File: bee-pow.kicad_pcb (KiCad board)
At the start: 2 copper layers, 29 x 53.3 mm, 12 parts, among them J1 Conn_01x02_Male, J2 Conn_01x02_Male, J3 Conn_01x02_Male, J4 Conn_01x02_Male

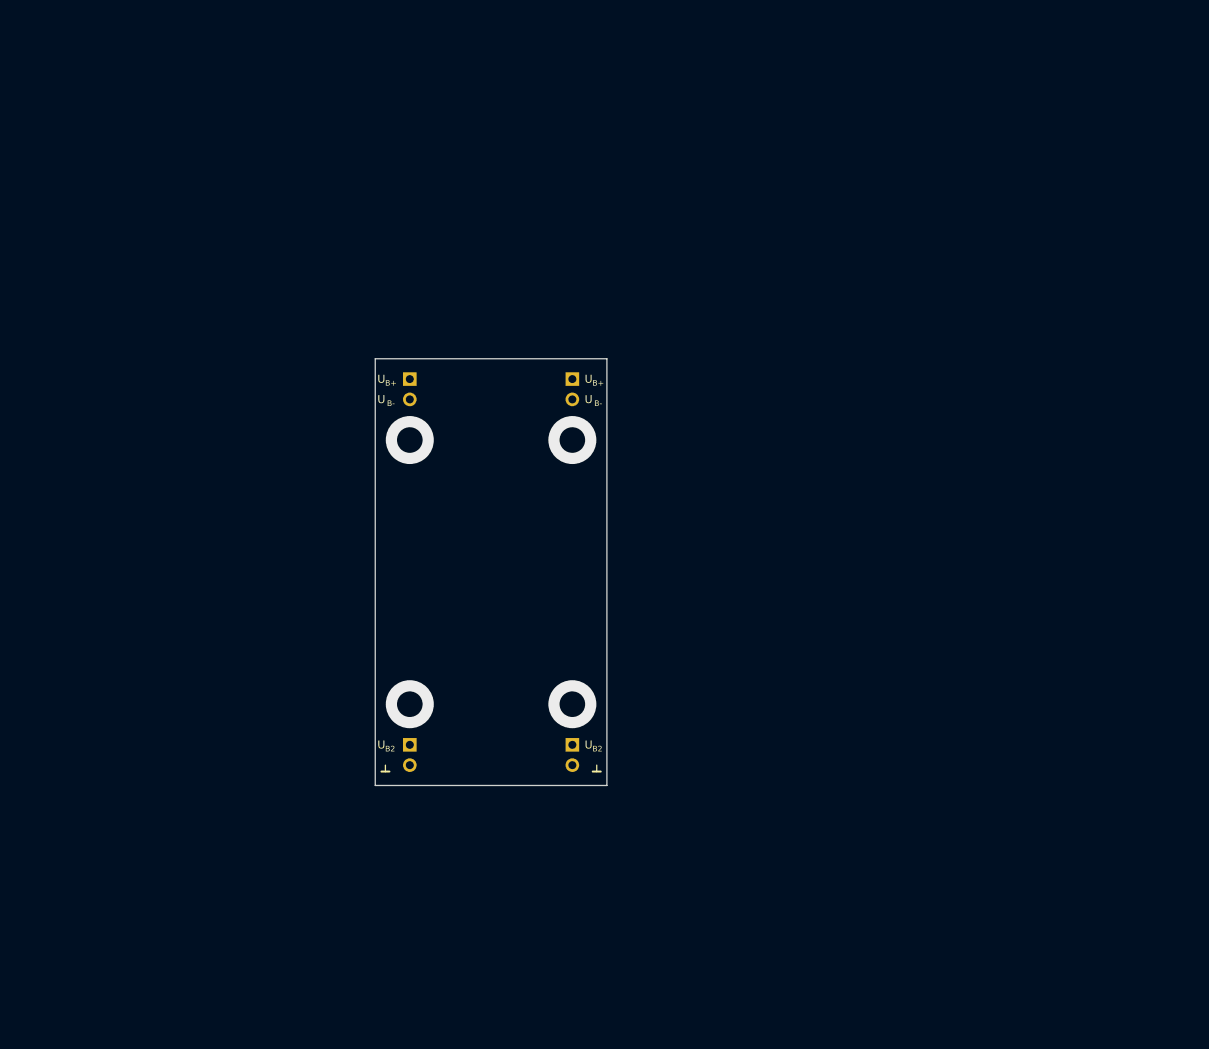
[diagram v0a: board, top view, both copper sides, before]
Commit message: begin schematic
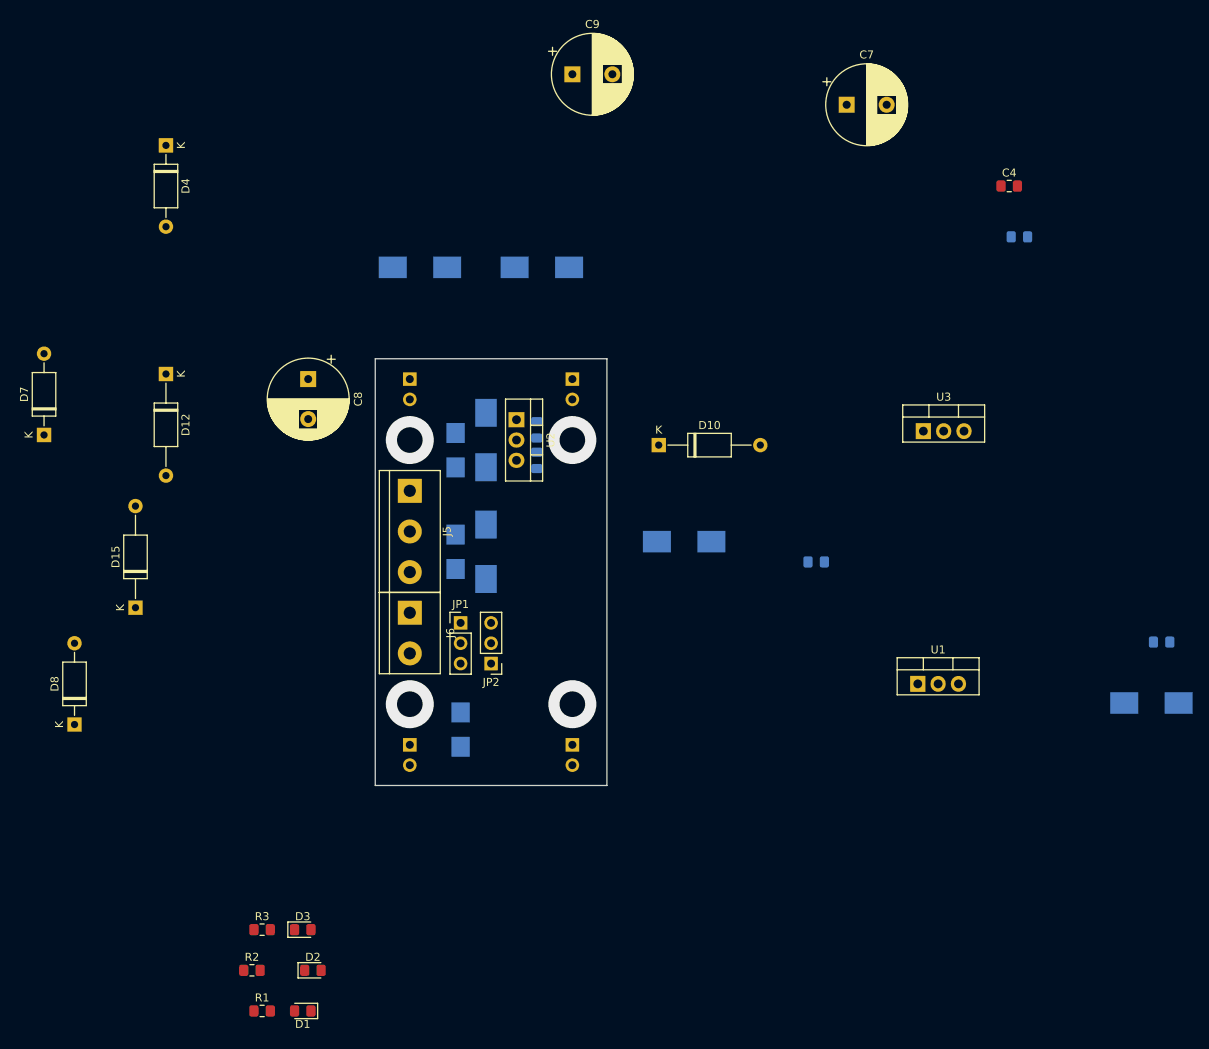
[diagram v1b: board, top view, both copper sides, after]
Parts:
- removed REF** (x2): Text_U_B+_Silkscreen, Symbol-emt:Text_U_B+_Silkscreen
- removed REF** (x2): Text_U_B-_Silkscreen, Symbol-emt:Text_U_B-_Silkscreen
- removed REF** (x2): Text_U_B2_Silkscreen, Symbol-emt:Text_U_B2_Silkscreen
- removed REF** (x2): Symbol_GND_Silkscreen, Symbol-emt:Symbol_GND_Silkscreen
- added C1: 0.33µF, Capacitor_SMD:C_0805_2012Metric_Pad1.15x1.40mm_HandSolder, B.Cu at (172.7, 124.3)
- added C2: 0.33µF, Capacitor_SMD:C_0805_2012Metric_Pad1.15x1.40mm_HandSolder, B.Cu at (94.6, 97.8)
- added C3: 0.33µF, Capacitor_SMD:C_0805_2012Metric_Pad1.15x1.40mm_HandSolder, B.Cu at (154.9, 73.7)
- added C4: 0.1µF, Capacitor_SMD:C_0805_2012Metric_Pad1.15x1.40mm_HandSolder, F.Cu at (153.7, 67.3)
- added C5: 0.1µF, Capacitor_SMD:C_0805_2012Metric_Pad1.15x1.40mm_HandSolder, B.Cu at (94.6, 101.6)
- added C6: 0.1µF, Capacitor_SMD:C_0805_2012Metric_Pad1.15x1.40mm_HandSolder, B.Cu at (129.5, 114.3)
- added C7: 220µF, Capacitor_THT:CP_Radial_D10.0mm_P5.00mm, F.Cu at (133.3, 57.1)
- added C8: 220µF, Capacitor_THT:CP_Radial_D10.0mm_P5.00mm, F.Cu at (66.0, 91.4)
- added C9: 220µF, Capacitor_THT:CP_Radial_D10.0mm_P5.00mm, F.Cu at (99.1, 53.3)
- added D1: LED, LED_SMD:LED_0805_2012Metric_Pad1.15x1.40mm_HandSolder, F.Cu at (65.4, 170.4)
- added D10: 1N4001, Diode_THT:D_A-405_P12.70mm_Horizontal, F.Cu at (109.9, 99.7)
- added D11: 1N4001, Diode_SMD:D_MELF_Handsoldering, B.Cu at (80.0, 77.5)
- added D12: 1N4001, Diode_THT:D_A-405_P12.70mm_Horizontal, F.Cu at (48.3, 90.8)
- added D13: 1N4001, Diode_SMD:D_MELF_Handsoldering, B.Cu at (88.3, 99.1)
- added D14: 1N4001, Diode_SMD:D_MELF_Handsoldering, B.Cu at (88.3, 113.0)
- added D15: 1N4001, Diode_THT:D_A-405_P12.70mm_Horizontal, F.Cu at (44.5, 120.0)
- added D16: 1N4001, Diode_SMD:D_MELF_Handsoldering, B.Cu at (95.2, 77.5)
- added D17: 1N4001, Diode_SMD:D_MELF_Handsoldering, B.Cu at (113.0, 111.8)
- added D18: 1N4001, Diode_SMD:D_MELF_Handsoldering, B.Cu at (171.4, 131.9)
- added D2: LED, LED_SMD:LED_0805_2012Metric_Pad1.15x1.40mm_HandSolder, F.Cu at (66.6, 165.3)
- added D3: LED, LED_SMD:LED_0805_2012Metric_Pad1.15x1.40mm_HandSolder, F.Cu at (65.4, 160.3)
- added D4: D_Schottky, Diode_THT:D_A-405_P10.16mm_Horizontal, F.Cu at (48.3, 62.2)
- added D5: D_Schottky, Diode_SMD:D_SMB, B.Cu at (84.5, 100.3)
- added D6: D_Schottky, Diode_SMD:D_SMB, B.Cu at (84.5, 113.0)
- added D7: D_Schottky, Diode_THT:D_A-405_P10.16mm_Horizontal, F.Cu at (33.0, 98.4)
- added D8: D_Schottky, Diode_THT:D_A-405_P10.16mm_Horizontal, F.Cu at (36.8, 134.6)
- added D9: D_Schottky, Diode_SMD:D_SMB, B.Cu at (85.1, 135.3)
- added J5: Screw_Terminal_01x03, TerminalBlock:TerminalBlock_bornier-3_P5.08mm, F.Cu at (78.7, 105.4)
- added J6: Screw_Terminal_01x02, TerminalBlock:TerminalBlock_bornier-2_P5.08mm, F.Cu at (78.7, 120.7)
- added JP1: Jumper_3_Bridged12, Connector_PinHeader_2.54mm:PinHeader_1x03_P2.54mm_Vertical, F.Cu at (85.1, 121.9)
- added JP2: Jumper_3_Bridged12, Connector_PinHeader_2.54mm:PinHeader_1x03_P2.54mm_Vertical, F.Cu at (88.9, 127.0)
- added R1: 1k5, Resistor_SMD:R_0805_2012Metric_Pad1.15x1.40mm_HandSolder, F.Cu at (60.3, 170.4)
- added R2: 1k5, Resistor_SMD:R_0805_2012Metric_Pad1.15x1.40mm_HandSolder, F.Cu at (59.0, 165.3)
- added R3: 330R, Resistor_SMD:R_0805_2012Metric_Pad1.15x1.40mm_HandSolder, F.Cu at (60.3, 160.3)
- added U1: L7805, Package_TO_SOT_THT:TO-220-3_Vertical, F.Cu at (142.2, 129.5)
- added U2: L7815, Package_TO_SOT_THT:TO-220-3_Vertical, F.Cu at (92.1, 96.5)
- added U3: L7915, Package_TO_SOT_THT:TO-220-3_Vertical, F.Cu at (142.9, 97.9)
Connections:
- net +15V renamed U_B+
- net +5V renamed U_B2
- net -15V renamed U_B-
